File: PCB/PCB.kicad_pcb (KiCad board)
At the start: 2 copper layers, 11 parts

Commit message: Routing & DRC of PCB
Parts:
- moved R1 44.7 mm to (117.1, 124.8)
- moved R4 24.6 mm to (117.1, 135.3)
- moved R2 23.6 mm to (117.6, 113.3)
- moved BZ1 21.3 mm to (159.5, 141.7)
- moved D2 19.6 mm to (163.3, 124.9)
- moved D3 19.6 mm to (163.3, 118.9)
- moved D1 19.6 mm to (163.3, 130.9)
- moved U3 17.8 mm to (167.0, 65.2)
- moved U2 17.2 mm to (163.5, 101.5)
- moved U1 16.2 mm to (140.4, 65.9)
- moved R3 10.0 mm to (117.6, 101.3)
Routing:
- net GND: track 0.00 -> 204.0 mm
- net Source: track 0.00 -> 99.8 mm, vias 0 -> 2
- net GREEN: track 0.00 -> 75.0 mm
- net Buzz: track 0.00 -> 70.8 mm
- net YELLOW: track 0.00 -> 69.4 mm
- net REDR: track 0.00 -> 68.4 mm
- net RED: track 0.00 -> 65.3 mm
- net CLK: track 0.00 -> 61.6 mm
- net Trigger: track 0.00 -> 52.4 mm
- net DIO: track 0.00 -> 46.2 mm
- net Echo: track 0.00 -> 30.4 mm
- net Net-(D3-A): track 0.00 -> 29.6 mm
- net Net-(D2-A): track 0.00 -> 26.3 mm
- net Net-(BZ1-+): track 0.00 -> 22.2 mm
- added copper zone on B.Cu, net GND
- added copper zone on F.Cu, net GND
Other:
- board outline added: 120.6 x 120.6 mm

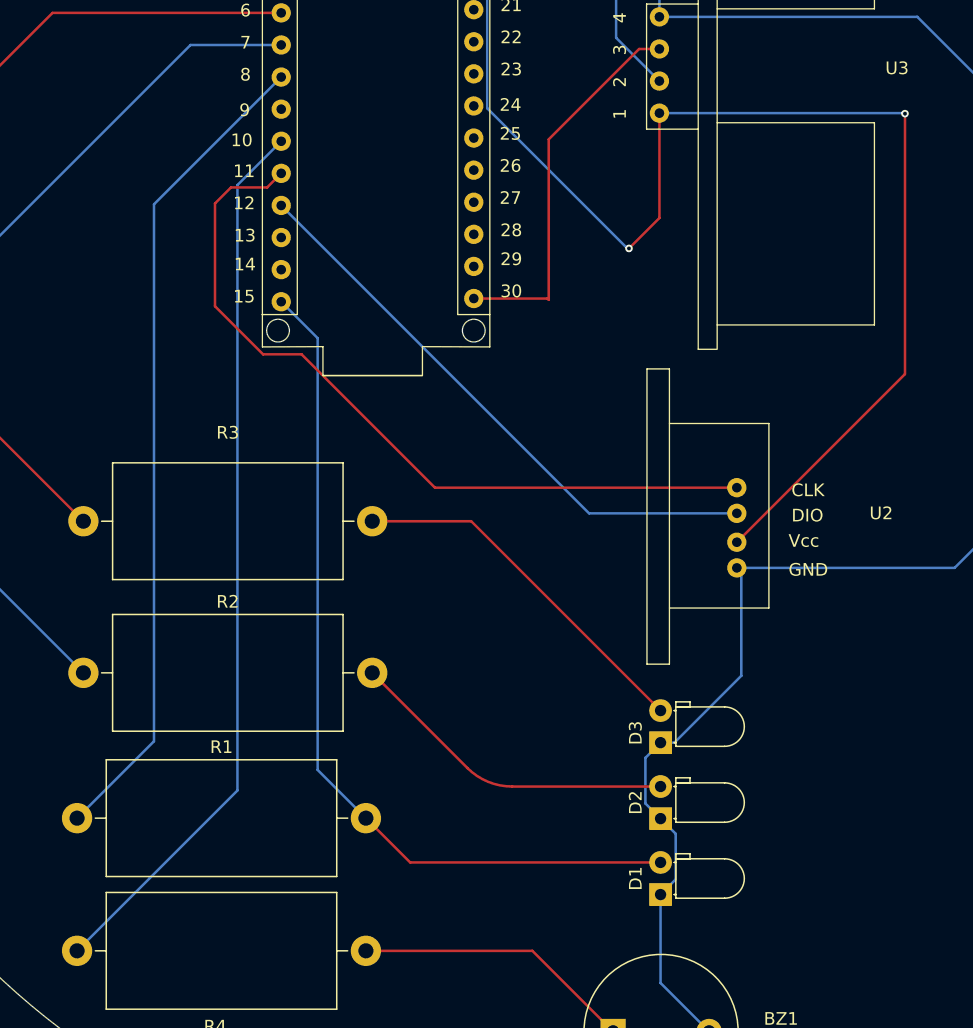
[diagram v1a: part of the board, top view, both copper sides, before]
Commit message: Additional changes to TM1637 footprint
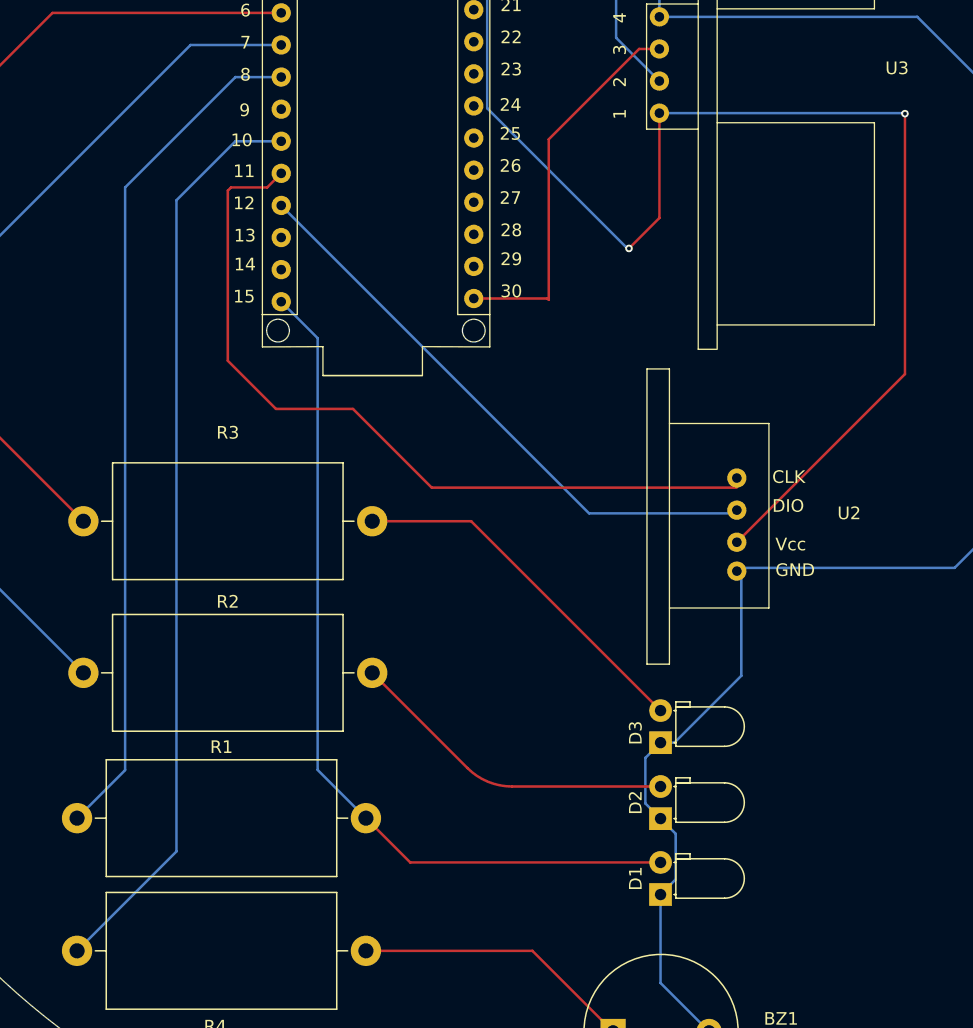
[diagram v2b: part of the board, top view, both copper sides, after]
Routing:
- net RED: track 65.3 -> 67.5 mm
- net Buzz: track 70.8 -> 72.9 mm
- net CLK: track 61.6 -> 62.7 mm
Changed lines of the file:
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@@
 	)
 	(paper "A4")
+	(title_block
+		(title "Traffic Lights")
+		(date "2024-12-23")
+		(company "Robotics'n'Circuits")
+	)
 	(layers
 		(0 "F.Cu" signal)
@@
 		(at 163.476 101.484)
 		(property "Reference" "U2"
-			(at 17.272 -0.762 0)
+			(at 14.732 -0.762 0)
 			(unlocked yes)
 			(layer "F.SilkS")
@@
 		)
 		(property "Value" "~"
-			(at 13.374 0.182 0)
+			(at 14.732 0.254 0)
 			(unlocked yes)
 			(layer "F.Fab")
@@
 		)
 		(fp_text user "Vcc"
-			(at 9.93 2.008 0)
+			(at 8.89 2.286 0)
 			(unlocked yes)
 			(layer "F.SilkS")
@@
 		)
 		(fp_text user "GND"
-			(at 9.93 4.294 0)
+			(at 8.89 4.318 0)
 			(unlocked yes)
 			(layer "F.SilkS")
@@
 		)
 		(fp_text user "CLK"
-			(at 10.16 -2 0)
+			(at 8.636 -3.048 0)
 			(unlocked yes)
 			(layer "F.SilkS")
@@
 		)
 		(fp_text user "DIO"
-			(at 10.16 0 0)
+			(at 8.636 -0.762 0)
 			(unlocked yes)
 			(layer "F.SilkS")
@@
 		)
 		(fp_text user "${REFERENCE}"
-			(at 21.59 1.27 0)
+			(at 17.78 1.524 0)
 			(unlocked yes)
 			(layer "F.Fab")
@@
 		)
 		(pad "1" thru_hole circle
-			(at 5.842 3.556)
+			(at 5.842 3.81)
 			(size 1.524 1.524)
 			(drill 0.762)
@@
 		)
 		(pad "3" thru_hole circle
-			(at 5.842 -0.762)
+			(at 5.842 -1.016)
 			(size 1.524 1.524)
 			(drill 0.762)
@@
 		)
 		(pad "4" thru_hole circle
-			(at 5.842 -2.794)
+			(at 5.842 -3.556)
 			(size 1.524 1.524)
 			(drill 0.762)
@@
 	(segment
 		(start 117.102 124.846)
-		(end 123.19 118.758)
+		(end 120.904 121.044)
 		(width 0.2)
 		(layer "B.Cu")
@@
 	)
 	(segment
-		(start 123.19 76.264)
+		(start 129.64 66.194)
 		(end 133.26 66.194)
 		(width 0.2)
@@
 	)
 	(segment
-		(start 123.19 118.758)
-		(end 123.19 76.264)
+		(start 120.904 74.93)
+		(end 129.64 66.194)
+		(width 0.2)
+		(layer "B.Cu")
+		(net 6)
+	)
+	(segment
+		(start 120.904 121.044)
+		(end 120.904 74.93)
 		(width 0.2)
 		(layer "B.Cu")
@@
 	)
 	(segment
+		(start 129.64 71.274)
+		(end 133.26 71.274)
+		(width 0.2)
+		(layer "B.Cu")
+		(net 9)
+	)
+	(segment
 		(start 117.102 135.346)
-		(end 129.794 122.654)
+		(end 124.968 127.48)
 		(width 0.2)
 		(layer "B.Cu")
@@
 	)
 	(segment
-		(start 129.794 122.654)
-		(end 129.794 74.74)
+		(start 124.968 75.946)
+		(end 129.64 71.274)
 		(width 0.2)
 		(layer "B.Cu")
@@
 	)
 	(segment
-		(start 129.794 74.74)
-		(end 133.26 71.274)
+		(start 124.968 127.48)
+		(end 124.968 75.946)
 		(width 0.2)
 		(layer "B.Cu")
@@
 	)
 	(segment
-		(start 128.016 76.2)
-		(end 129.286 74.93)
+		(start 129.032 88.646)
+		(end 129.032 75.184)
 		(width 0.2)
 		(layer "F.Cu")
@@
 	)
 	(segment
-		(start 132.144 74.93)
-		(end 133.26 73.814)
+		(start 129.286 74.93)
+		(end 132.144 74.93)
 		(width 0.2)
 		(layer "F.Cu")
@@
 	)
 	(segment
-		(start 129.286 74.93)
-		(end 132.144 74.93)
+		(start 169.318 98.69)
+		(end 145.172 98.69)
 		(width 0.2)
 		(layer "F.Cu")
@@
 	)
 	(segment
-		(start 134.874 88.138)
-		(end 131.826 88.138)
+		(start 138.938 92.456)
+		(end 132.842 92.456)
 		(width 0.2)
 		(layer "F.Cu")
@@
 	)
 	(segment
-		(start 131.826 88.138)
-		(end 128.016 84.328)
+		(start 132.842 92.456)
+		(end 129.032 88.646)
 		(width 0.2)
 		(layer "F.Cu")
@@
 	)
 	(segment
-		(start 145.426 98.69)
-		(end 134.874 88.138)
+		(start 129.032 75.184)
+		(end 129.286 74.93)
 		(width 0.2)
 		(layer "F.Cu")
@@
 	)
 	(segment
-		(start 169.318 98.69)
-		(end 145.426 98.69)
+		(start 145.172 98.69)
+		(end 138.938 92.456)
 		(width 0.2)
 		(layer "F.Cu")
@@
 	)
 	(segment
-		(start 128.016 84.328)
-		(end 128.016 76.2)
+		(start 132.144 74.93)
+		(end 133.26 73.814)
 		(width 0.2)
 		(layer "F.Cu")
